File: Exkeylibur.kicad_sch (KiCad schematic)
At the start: 24 parts, among them J1 TRRS, SW1 SW_Push, SW10 SW_Push, SW11 SW_Push, SW12 SW_Push, SW13 SW_Push, SW14 SW_Push, SW15 SW_Push, SW16 SW_Push, SW17 SW_Push, SW18 SW_Push, SW19 SW_Push, SW2 SW_Push, SW20 SW_Push, SW3 SW_Push, SW4 SW_Push, SW5 SW_Push, SW6 SW_Push, SW7 SW_Push, SW8 SW_Push, SW9 SW_Push, U1 Elite-C

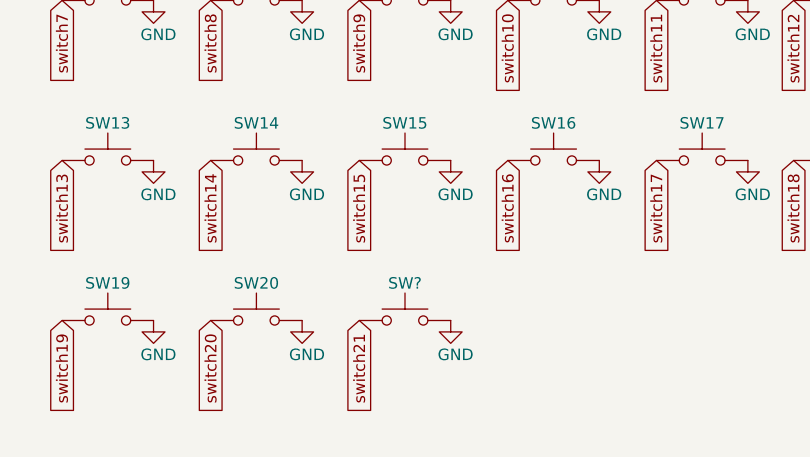
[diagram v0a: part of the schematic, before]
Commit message: typo fix on switch ref des
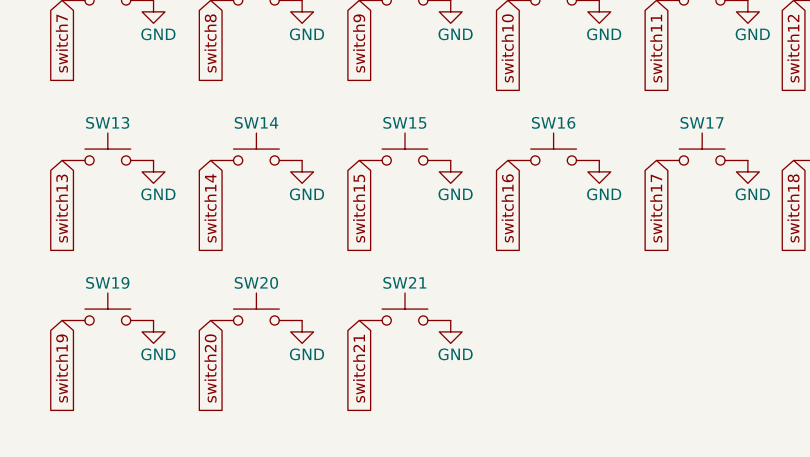
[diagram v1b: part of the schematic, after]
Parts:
- gave numbers to parts that had none: 1
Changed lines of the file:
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@@
   (symbol (lib_id "Switch:SW_Push") (at 227.33 71.12 0) (unit 1)
     (in_bom yes) (on_board yes)
-    (property "Reference" "SW?" (id 0) (at 227.33 66.99 0))
+    (property "Reference" "SW21" (id 0) (at 227.33 66.99 0))
     (property "Value" "SW_Push" (id 1) (at 227.33 67.31 0)
       (effects (font (size 1.27 1.27)) hide)
@@
     )
     (path "/db4ecfa9-7af4-4d96-acaa-0f6fe7a9e781"
-      (reference "SW?") (unit 1) (value "SW_Push") (footprint "")
+      (reference "SW21") (unit 1) (value "SW_Push") (footprint "")
     )
     (path "/0eff0d29-daaf-429c-af88-ce7c3ea9c3ba"

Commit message: connect OLED to MC
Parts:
- added D1: OLED_128_32, symbol OLED:OLED_128_32
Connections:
- net at U1.5 (2/PD1/SDA): now also D1.1 (SDA)
- net at U1.6 (3/PD0/SCL): now also D1.2 (SCL)
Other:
- moved on the sheet: J1
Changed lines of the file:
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@@
   (junction (at 113.03 30.48) (diameter 0) (color 0 0 0 0)
+  )
+  (wire (pts (xy 100.33 25.4) (xy 100.33 19.05))
+    (stroke (width 0) (type default) (color 0 0 0 0))
   )
   (wire (pts (xy 113.03 27.94) (xy 113.03 30.48))
@@
     (stroke (width 0) (type default) (color 0 0 0 0))
   )
+  (wire (pts (xy 116.84 25.4) (xy 100.33 25.4))
+    (stroke (width 0) (type default) (color 0 0 0 0))
+  )
   (wire (pts (xy 179.07 19.05) (xy 177.8 19.05))
     (stroke (width 0) (type default) (color 0 0 0 0))
@@
     (stroke (width 0) (type default) (color 0 0 0 0))
   )
-  (wire (pts (xy 77.47 20.32) (xy 92.71 20.32))
+  (wire (pts (xy 66.04 19.05) (xy 100.33 19.05))
     (stroke (width 0) (type default) (color 0 0 0 0))
   )
@@
     (stroke (width 0) (type solid) (color 0 0 0 0))
   )
-  (wire (pts (xy 116.84 25.4) (xy 92.71 25.4))
+  (wire (pts (xy 93.98 33.02) (xy 116.84 33.02))
     (stroke (width 0) (type default) (color 0 0 0 0))
   )
-  (wire (pts (xy 92.71 25.4) (xy 92.71 20.32))
+  (wire (pts (xy 93.98 35.56) (xy 116.84 35.56))
     (stroke (width 0) (type default) (color 0 0 0 0))
   )
@@
     (effects (font (size 1.27 1.27)) (justify left bottom))
   )
-  (label "DATA" (at 81.28 20.32 0)
+  (label "DATA" (at 69.85 19.05 0)
     (effects (font (size 1.27 1.27)) (justify left bottom))
   )
@@
     (pin "2")
   )
+  (symbol (lib_id "OLED:OLED_128_32") (at 85.09 29.21 0) (unit 1)
+    (in_bom yes) (on_board yes)
+    (property "Reference" "D1" (id 0) (at 85.09 26.67 0))
+    (property "Value" "OLED_128_32" (id 1) (at 85.09 29.21 0))
+    (property "Footprint" "" (id 2) (at 85.09 29.21 0)
+      (effects (font (size 1.27 1.27)) hide)
+    )
+    (property "Datasheet" "" (id 3) (at 85.09 29.21 0)
+      (effects (font (size 1.27 1.27)) hide)
+    )
+    (pin "1")
+    (pin "2")
+    (pin "3")
+    (pin "4")
+  )
   (symbol (lib_id "Switch:SW_Push") (at 194.31 35.56 0) (unit 1)
     (in_bom yes) (on_board yes)
@@
     (pin "1")
   )
-  (symbol (lib_id "power:GND") (at 77.47 22.86 90) (unit 1)
-    (in_bom yes) (on_board yes)
-    (property "Reference" "#PWR?" (id 0) (at 83.82 22.86 0)
-      (effects (font (size 1.27 1.27)) hide)
-    )
-    (property "Value" "GND" (id 1) (at 80.01 22.86 90)
-      (effects (font (size 1.27 1.27)) (justify right))
-    )
-    (property "Footprint" "" (id 2) (at 77.47 22.86 0)
-      (effects (font (size 1.27 1.27)) hide)
-    )
-    (property "Datasheet" "" (id 3) (at 77.47 22.86 0)
+  (symbol (lib_id "power:GND") (at 66.04 21.59 90) (unit 1)
+    (in_bom yes) (on_board yes)
+    (property "Reference" "#PWR?" (id 0) (at 72.39 21.59 0)
+      (effects (font (size 1.27 1.27)) hide)
+    )
+    (property "Value" "GND" (id 1) (at 68.58 21.59 90)
+      (effects (font (size 1.27 1.27)) (justify right))
+    )
+    (property "Footprint" "" (id 2) (at 66.04 21.59 0)
+      (effects (font (size 1.27 1.27)) hide)
+    )
+    (property "Datasheet" "" (id 3) (at 66.04 21.59 0)
       (effects (font (size 1.27 1.27)) hide)
     )
@@
     (pin "1")
   )
-  (symbol (lib_id "power:VCC") (at 77.47 25.4 270) (unit 1)
-    (in_bom yes) (on_board yes)
-    (property "Reference" "#PWR?" (id 0) (at 73.66 25.4 0)
-      (effects (font (size 1.27 1.27)) hide)
-    )
-    (property "Value" "VCC" (id 1) (at 80.01 25.4 90)
+  (symbol (lib_id "power:VCC") (at 66.04 24.13 270) (unit 1)
+    (in_bom yes) (on_board yes)
+    (property "Reference" "#PWR?" (id 0) (at 62.23 24.13 0)
+      (effects (font (size 1.27 1.27)) hide)
+    )
+    (property "Value" "VCC" (id 1) (at 68.58 24.13 90)
       (effects (font (size 1.27 1.27)) (justify left))
     )
-    (property "Footprint" "" (id 2) (at 77.47 25.4 0)
-      (effects (font (size 1.27 1.27)) hide)
-    )
-    (property "Datasheet" "" (id 3) (at 77.47 25.4 0)
+    (property "Footprint" "" (id 2) (at 66.04 24.13 0)
+      (effects (font (size 1.27 1.27)) hide)
+    )
+    (property "Datasheet" "" (id 3) (at 66.04 24.13 0)
       (effects (font (size 1.27 1.27)) hide)
     )
@@
     (pin "1")
   )
-  (symbol (lib_id "Connector:AudioJack4") (at 72.39 22.86 0) (unit 1)
-    (in_bom yes) (on_board yes)
-    (property "Reference" "J1" (id 0) (at 69.85 13.97 0))
-    (property "Value" "TRRS" (id 1) (at 69.85 16.51 0))
-    (property "Footprint" "" (id 2) (at 72.39 22.86 0)
-      (effects (font (size 1.27 1.27)) hide)
-    )
-    (property "Datasheet" "~" (id 3) (at 72.39 22.86 0)
+  (symbol (lib_id "Connector:AudioJack4") (at 60.96 21.59 0) (unit 1)
+    (in_bom yes) (on_board yes)
+    (property "Reference" "J1" (id 0) (at 58.42 14.22 0))
+    (property "Value" "TRRS" (id 1) (at 58.42 16.51 0))
+    (property "Footprint" "" (id 2) (at 60.96 21.59 0)
+      (effects (font (size 1.27 1.27)) hide)
+    )
+    (property "Datasheet" "~" (id 3) (at 60.96 21.59 0)
       (effects (font (size 1.27 1.27)) hide)
     )
@@
       (reference "#PWR?") (unit 1) (value "GND") (footprint "")
     )
+    (path "/65f43e89-4033-45fc-ba02-71b697a697aa"
+      (reference "D1") (unit 1) (value "OLED_128_32") (footprint "")
+    )
     (path "/f07452ad-0380-41f1-a120-c6a4d5addbd1"

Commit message: make right side schematic
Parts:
- added D2: OLED, symbol OLED:OLED_128_32
- added J2: TRRS, symbol Connector:AudioJack4
- added RSW2, SW22, SW23, SW24, SW25, SW26, SW27, SW28, SW29, SW30, SW31, SW32, SW33, SW34, SW35, SW36, SW37, SW38, SW39, SW40, SW41, SW42: SW_Push, symbol Switch:SW_Push
- added U2: Elite-C, Elite_C:Elite-C, symbol keebio:Elite-C
- D1: value OLED_128_32 -> OLED
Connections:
- net GND: now also D1.4 (GND), D2.4 (GND), J2.R2, RSW2.2, SW22.2, SW23.2, SW24.2, SW25.2, SW26.2, SW27.2, SW28.2, SW29.2, SW30.2, SW31.2, SW32.2, SW33.2, SW34.2, SW35.2, SW36.2, SW37.2, SW38.2, SW39.2, SW40.2, SW41.2, SW42.2, U2.23 (GND), U2.3 (GND), U2.4 (GND)
- net VCC: now also D1.3 (VCC), D2.3 (VCC), J2.R1, U2.21 (VCC)
- new net: D2.1 (SDA), U2.5 (2/PD1/SDA)
- new net: D2.2 (SCL), U2.6 (3/PD0/SCL)
- new net DATA_R: J2.S, U2.2 (RX1/PD2)
- new net RST_R: RSW2.1, U2.22 (RST)
- new net switch10_r: SW31.1, U2.7 (4/PD4)
- new net switch11_r: SW32.1, U2.8 (5/PC6)
- new net switch12_r: SW33.1, U2.1 (TX0/PD3)
- new net switch13_r: SW34.1, U2.9 (6/PD7)
- new net switch14_r: SW35.1, U2.10 (7/PE6)
- new net switch15_r: SW36.1, U2.11 (8/PB4)
- new net switch16_r: SW37.1, U2.12 (9/PB5)
- new net switch17_r: SW38.1, U2.29 (F0)
- new net switch18_r: SW39.1, U2.28 (F1)
- new net switch19_r: SW40.1, U2.27 (C7)
- new net switch1_r: SW22.1, U2.24 (B0)
- new net switch20_r: SW41.1, U2.26 (D5)
- new net switch21_r: SW42.1, U2.25 (B7)
- new net switch2_2: SW23.1
- new net switch2_r: U2.20 (A3/PF4)
- new net switch3_r: SW24.1, U2.19 (A2/PF5)
- new net switch4_r: SW25.1, U2.18 (A1/PF6)
- new net switch5_r: SW26.1, U2.17 (A0/PF7)
- new net switch6_r: SW27.1, U2.16 (15/PB1)
- new net switch7_r: SW28.1, U2.15 (14/PB3)
- new net switch8_r: SW29.1, U2.14 (16/PB2)
- new net switch9_r: SW30.1, U2.13 (10/PB6)
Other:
- moved on the sheet: D1, J1, RSW1, SW1, SW10, SW11, SW12, SW13, SW14, SW15, SW16, SW17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
